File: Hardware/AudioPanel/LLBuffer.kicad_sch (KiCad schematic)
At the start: 13 parts, among them U3 NE5532

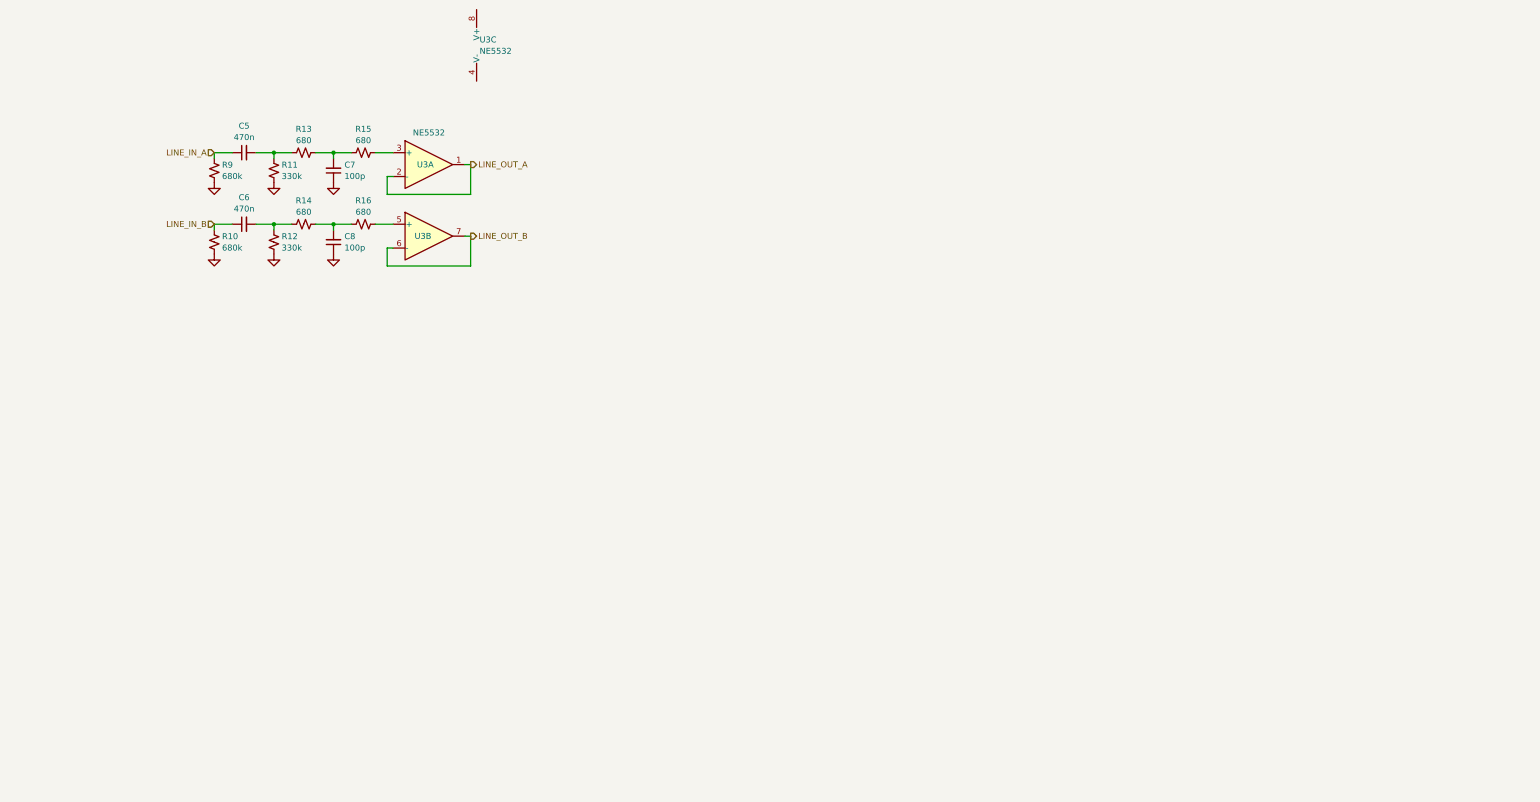
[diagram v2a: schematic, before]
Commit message: Revisiting the audio input buffer circuit
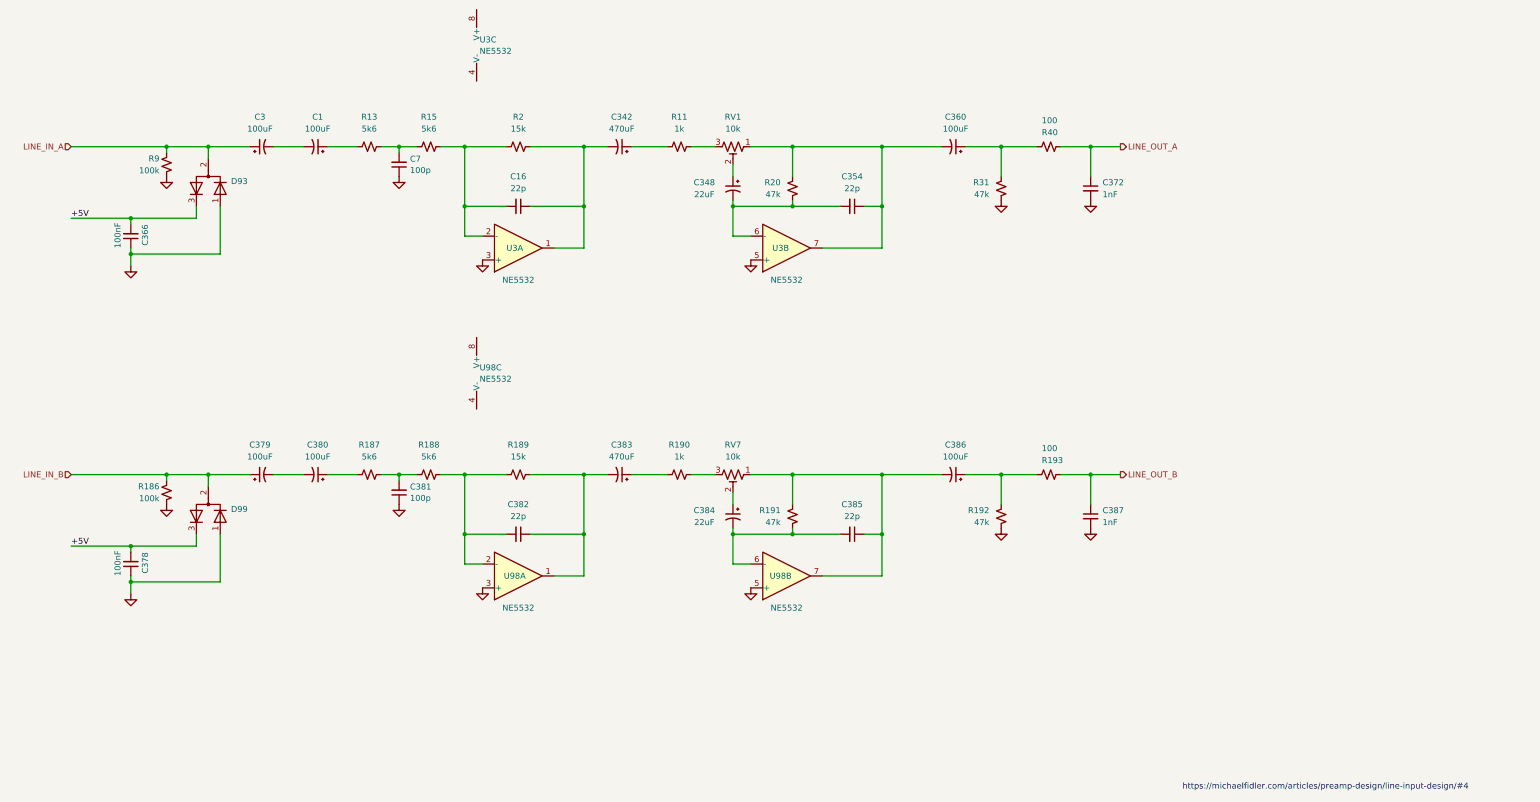
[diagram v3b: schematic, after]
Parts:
- removed C5, C6: 470n, symbol Device:C_Small
- removed C8: 100p, symbol Device:C_Small
- removed R10: 680k, symbol Device:R_Small_US
- removed R12: 330k, symbol Device:R_Small_US
- removed R14, R16: 680, symbol Device:R_Small_US
- added C1, C3, C360, C379, C380, C386: 100uF, symbol Device:C_Polarized_Small_US
- added C16, C354, C382, C385: 22p, symbol Device:C_Small
- added C342, C383: 470uF, symbol Device:C_Polarized_Small_US
- added C348, C384: 22uF, symbol Device:C_Polarized_Small_US
- added C366, C378: 100nF, symbol Device:C_Small
- added C372, C387: 1nF, symbol Device:C_Small
- added C381: 100p, symbol Device:C_Small
- added D93, D99: D_Dual_Series_ACK_Parallel, symbol Device:D_Dual_Series_ACK_Parallel
- added R186: 100k, symbol Device:R_Small_US
- added R187, R188: 5k6, symbol Device:R_Small_US
- added R189, R2: 15k, symbol Device:R_Small_US
- added R190: 1k, symbol Device:R_Small_US
- added R191, R192, R20, R31: 47k, symbol Device:R_Small_US
- added R193, R40: 100, symbol Device:R_Small_US
- added RV1, RV7: 10k, symbol Device:R_Potentiometer_Trim_US
- added U98: NE5532, symbol Amplifier_Operational:NE5532
- R11: value 330k -> 1k
- R13, R15: value 680 -> 5k6
- R9: value 680k -> 100k
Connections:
- net GND: now also U3.3 (+), U3.5 (+), C366.1, C372.2, C378.1, C381.1, C387.2, D93.1 (A), D99.1 (A), R186.2, R192.1, R31.1, U98.3 (+), U98.5 (+); no longer R11.2
- net LINE_IN_A: now also C3.1, D93.2 (common)
- net LINE_IN_B: now also C379.1, D99.2 (common), R186.1
- net LINE_OUT_A: now also C372.1, R40.2; no longer U3.1, U3.2 (-)
- net LINE_OUT_B: now also C387.1, R193.2; no longer U3.6 (-), U3.7
- net at R15.2: now also U3.2 (-), C16.2, R2.1; no longer U3.3 (+)
- net at R11.1: now also C342.1; no longer R13.1
- new net: C354.1, C360.2, R20.2, RV1.1, U3.7
- new net: C348.2, C354.2, R20.1, U3.6 (-)
- new net: R11.2, RV1.3
- new net: C16.1, C342.2, R2.2, U3.1
- new net: C386.1, R192.2, R193.1
- new net: C382.1, C383.2, R189.2, U98.1
- new net: C382.2, R188.2, R189.1, U98.2 (-)
- new net: C381.2, R187.2, R188.1
- new net: C379.2, C380.2
- new net: C1.1, R13.1
- new net: C1.2, C3.2
- new net: C348.1, RV1.2
- new net: C380.1, R187.1
- new net: C385.1, C386.2, R191.2, RV7.1, U98.7
- new net: C384.1, RV7.2
- new net: R190.2, RV7.3
- new net: C384.2, C385.2, R191.1, U98.6 (-)
- new net: C360.1, R31.2, R40.1
- new net: C383.1, R190.1
- new net +5V: C366.2, C378.2, D93.3 (K), D99.3 (K)
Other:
- note added: "https://michaelfidler.com/articles/preamp-design/line-input-design/#4"
- moved on the sheet: C7, R13, R15, R9, U3A, U3B

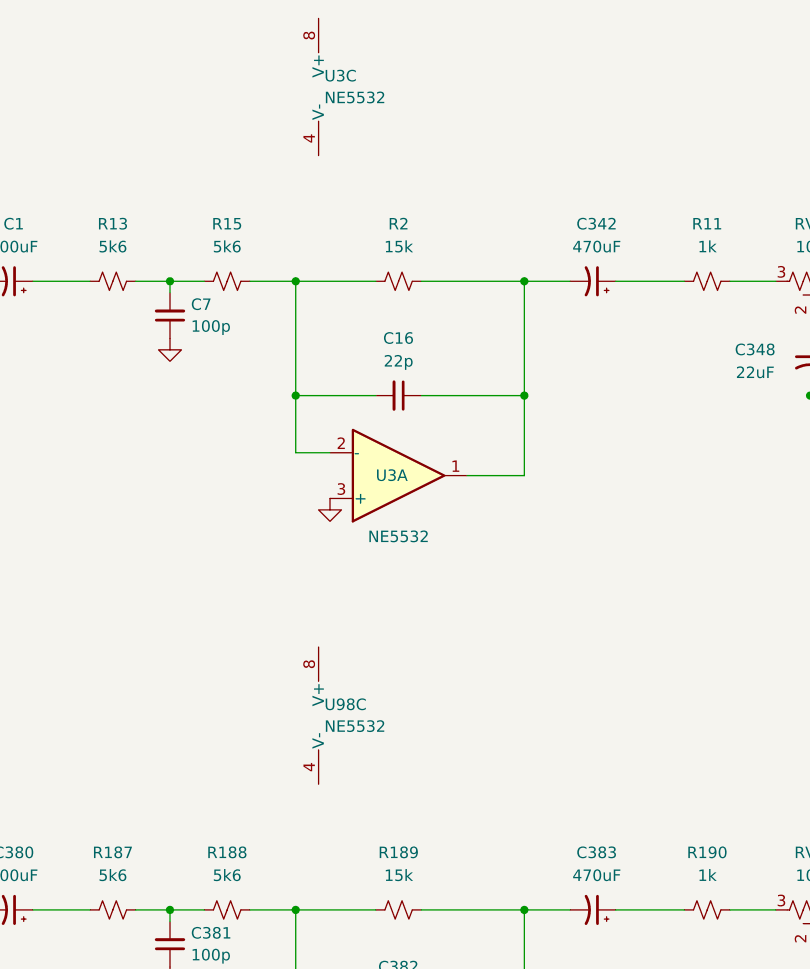
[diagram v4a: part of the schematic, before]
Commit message: Added main +5V supply with current sensing
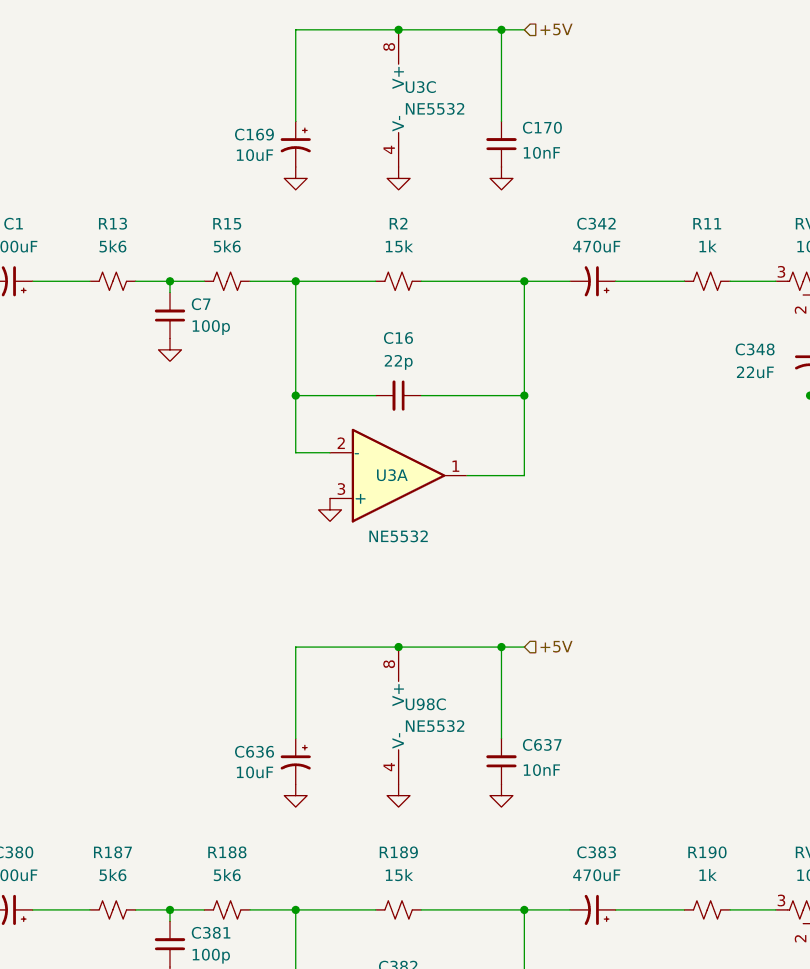
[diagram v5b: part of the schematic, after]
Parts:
- added C169, C636: 10uF, symbol Device:C_Polarized_Small_US
- added C170, C637: 10nF, symbol Device:C_Small
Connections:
- net +5V: now also U3.8 (V+), U98.8 (V+), C169.1, C170.2, C636.1, C637.2
- net GND: now also U3.4 (V-), U98.4 (V-), C169.2, C170.1, C636.2, C637.1
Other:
- moved on the sheet: U3C, U98C

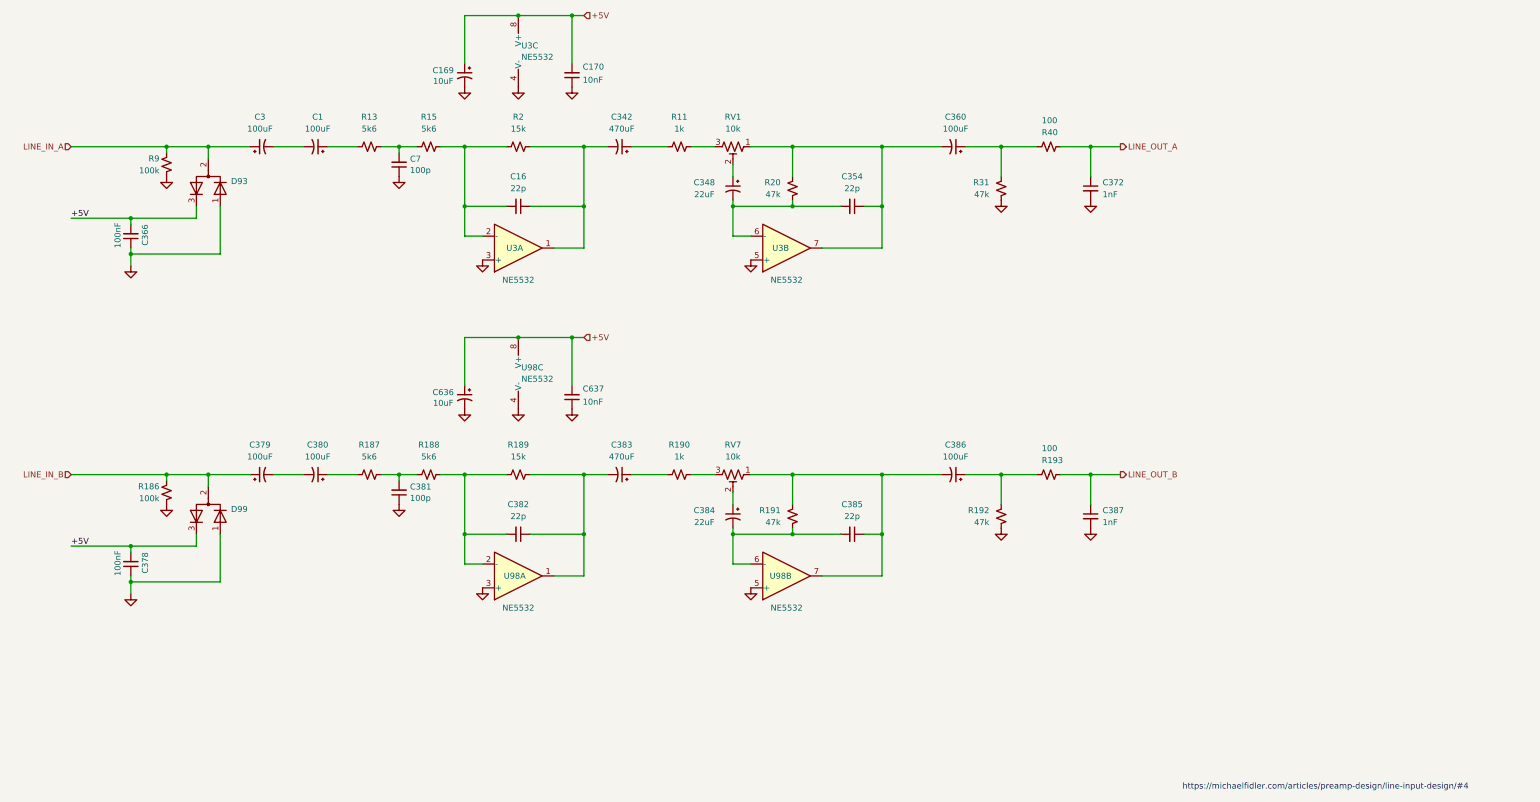
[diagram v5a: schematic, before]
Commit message: Realized that I need to rethink how I'm going to mix the radio audio with the stereo audio
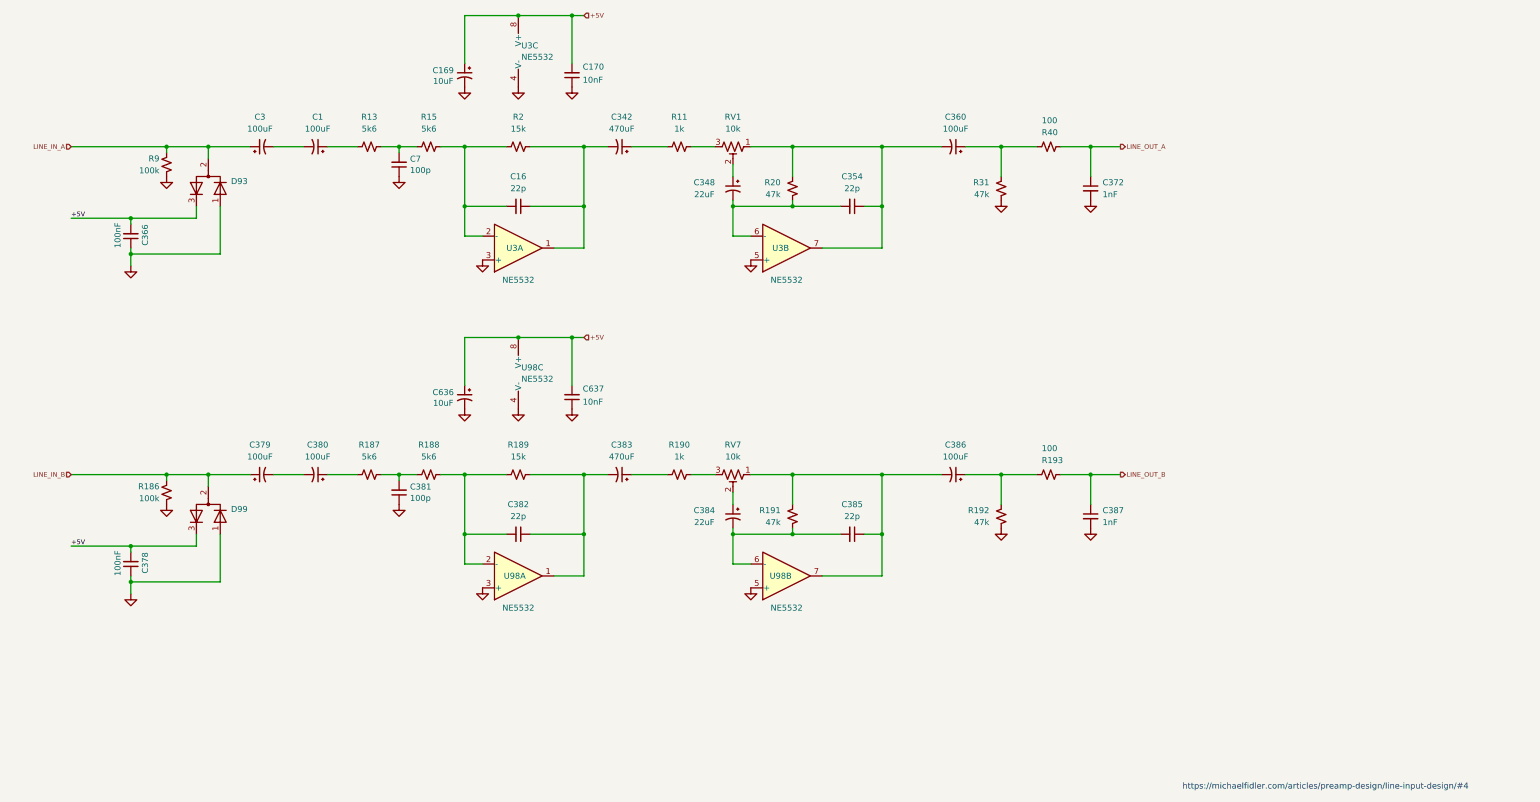
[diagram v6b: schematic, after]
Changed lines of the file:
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@@
 		(effects
 			(font
-				(size 1.27 1.27)
+				(size 1 1)
 			)
 			(justify left bottom)
@@
 		(effects
 			(font
-				(size 1.27 1.27)
+				(size 1 1)
 			)
 			(justify left bottom)
@@
 		(effects
 			(font
-				(size 1.27 1.27)
+				(size 1 1)
 				(color 105 14 0 1)
 			)
@@
 		(effects
 			(font
-				(size 1.27 1.27)
+				(size 1 1)
 			)
 			(justify left)
@@
 		(effects
 			(font
-				(size 1.27 1.27)
+				(size 1 1)
 			)
 			(justify left)
@@
 		(effects
 			(font
-				(size 1.27 1.27)
+				(size 1 1)
 				(color 105 14 0 1)
 			)
@@
 		(effects
 			(font
-				(size 1.27 1.27)
+				(size 1 1)
 				(color 105 14 0 1)
 			)
@@
 		(effects
 			(font
-				(size 1.27 1.27)
+				(size 1 1)
 				(color 105 14 0 1)
 			)
